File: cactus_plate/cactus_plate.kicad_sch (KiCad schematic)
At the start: 28 parts, among them J1 397730002, J2 397730002, J3 397730002, J4 Conn_01x04_Pin, K3 G2RL-1, K4 G2RL-2, Q1 BC337, Q2 BC337, U1 MT3608

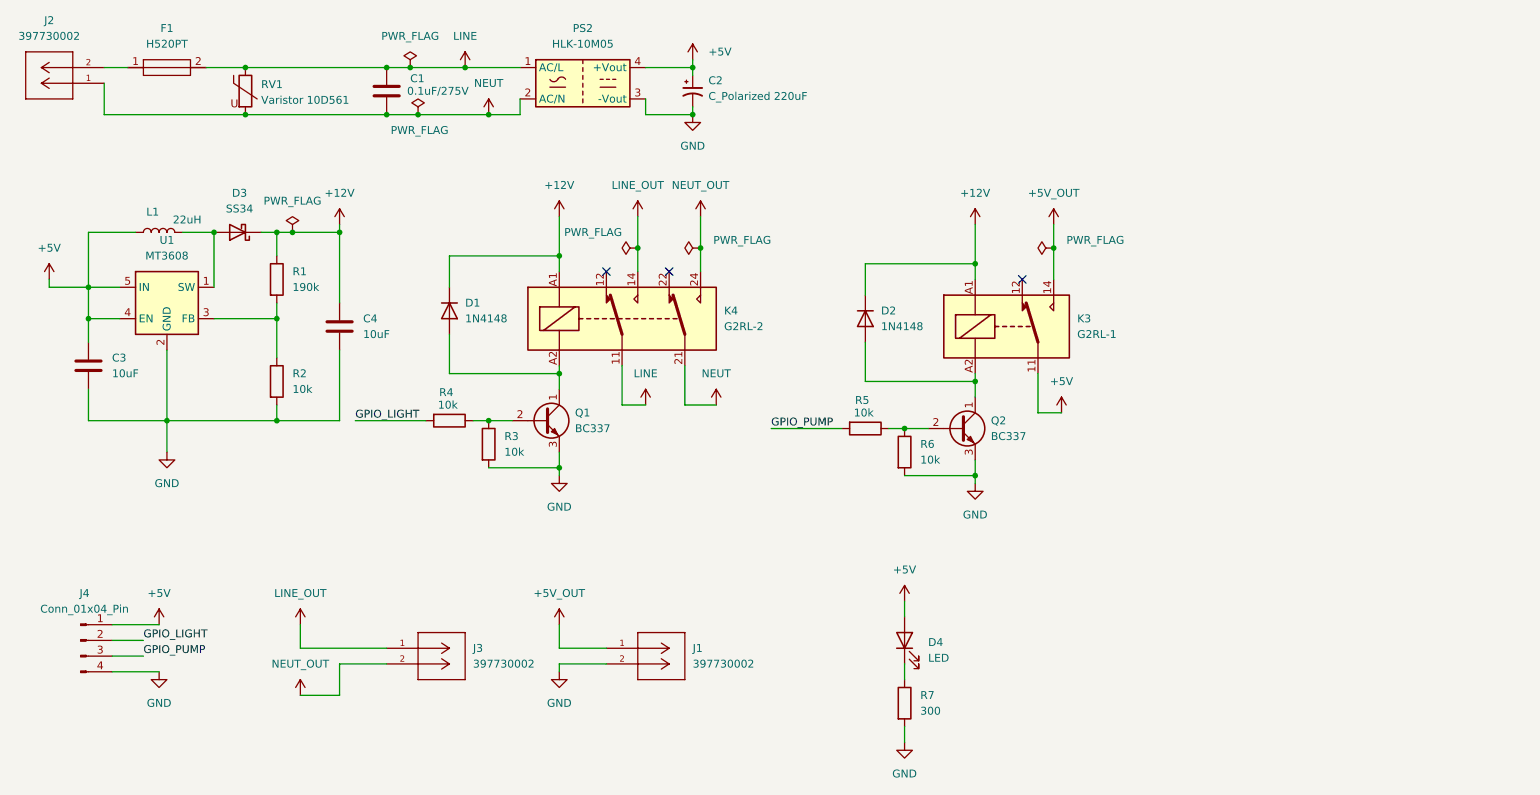
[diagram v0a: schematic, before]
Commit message: Переделал плату, добавил разъем для подсветки
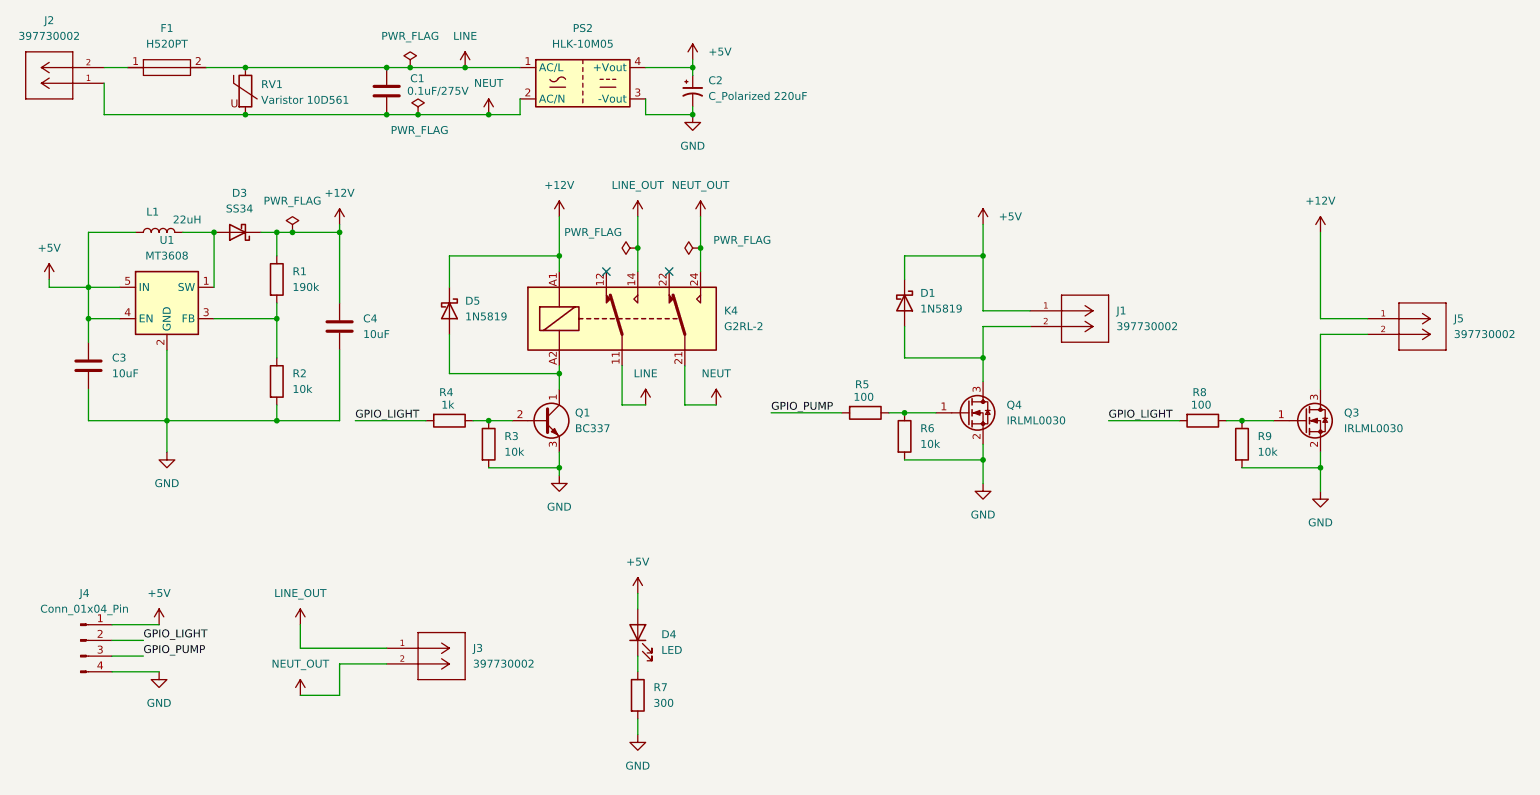
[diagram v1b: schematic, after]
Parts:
- removed D1, D2: 1N4148, Diode_THT:D_DO-35_SOD27_P7.62mm_Horizontal, symbol Diode:1N4148
- removed K3: G2RL-1, Relay_THT:Relay_SPDT_Omron_G2RL-1, symbol Relay:G2RL-1
- removed Q2: BC337, Package_TO_SOT_THT:TO-92_Inline, symbol Transistor_BJT:BC337
- added D1, D5: 1N5819, Diode_THT:D_DO-41_SOD81_P10.16mm_Horizontal, symbol Diode:1N5819
- added J5: 397730002, Connector_Phoenix_MC_HighVoltage:PhoenixContact_MCV_1,5_2-G-5.08_1x02_P5.08mm_Vertical, symbol MyLib:397730002
- added Q3, Q4: IRLML0030, Package_TO_SOT_SMD:SOT-23, symbol Transistor_FET:IRLML0030
- added R8: 100, Resistor_SMD:R_0805_2012Metric_Pad1.20x1.40mm_HandSolder, symbol Device:R
- added R9: 10k, Resistor_SMD:R_0805_2012Metric_Pad1.20x1.40mm_HandSolder, symbol Device:R
- R4: value 10k -> 1k
- R5: value 10k -> 100
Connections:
- net +5V_OUT is gone; now on net +5V: J1.1
- net +12V: now also D5.1 (K), J5.1
- net +5V: now also D1.1 (K)
- net GND: now also Q3.2 (S), Q4.2 (S), R9.2; no longer J1.2
- net GPIO_LIGHT: now also R8.2
- net at R5.1, R6.1: now also Q4.1 (G)
- net at K4.A2, Q1.1 (C): now also D5.2 (A)
- new net: D1.2 (A), J1.2, Q4.3 (D)
- new net: Q3.1 (G), R8.1, R9.1
- new net: J5.2, Q3.3 (D)
- no-connect marks 3 -> 2
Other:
- moved on the sheet: D4, J1, R5, R6, R7
